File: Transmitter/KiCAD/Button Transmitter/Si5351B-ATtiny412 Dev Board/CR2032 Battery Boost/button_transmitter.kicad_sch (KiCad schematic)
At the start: 35 parts, among them J1 1.27mm Pogo Pads, J2 Conn_Coaxial, Q1 MMUN2238LT1G, U1 ATtiny412-SS, U2 Si5351B-B-GM1, U3 TLV61070ADBV, Y1 25MHz

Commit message: Finished CR2032 PCB layout
I like this. This is good
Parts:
- removed BZ1: Buzzer Pads, Jumper:SolderJumper-2_P1.3mm_Open_RoundedPad1.0x1.5mm, symbol Device:Buzzer
- removed D2: LS0504EVT233, Package_TO_SOT_SMD:SOT-23-3, symbol Power_Protection:CM1213A-01SO
- removed U1: ATtiny412-SS, Package_SO:SOIC-8_3.9x4.9mm_P1.27mm, symbol MCU_Microchip_ATtiny:ATtiny412-SS
- added BZ1: 7BB-20-3, Library:Buzzer_Pad_POS, symbol library:Buzzer_Pad_POS
- added BZ2-1: 7BB-20-3, Library:Buzzer_Pad_NEG, symbol library:Buzzer_Pad_NEG
- added C7: 100nF, Library:Worthington_C_0402_1005Metric, symbol Device:C_Small
- added D2: ESD156B1W, Diode_SMD:D_0201_0603Metric, symbol Device:D_TVS
- added U1: TPS22919DCK, Package_TO_SOT_SMD:SOT-363_SC-70-6, symbol library:TPS22919DCK
- added U3: ATtiny416-M, Package_DFN_QFN:VQFN-20-1EP_3x3mm_P0.4mm_EP1.7x1.7mm, symbol MCU_Microchip_ATtiny:ATtiny416-M
- BT1: footprint Battery:BatteryHolder_Keystone_3034_1x20mm -> Library:BatteryHolder_Keystone_3034_1x20mm_CUTOUT
- C1: renamed from C3; footprint Resistor_SMD:R_0402_1005Metric -> Library:Worthington_C_0402_1005Metric
- C10: renamed from C9; footprint Resistor_SMD:R_0603_1608Metric -> Capacitor_SMD:C_0603_1608Metric
- C2: renamed from C4; footprint Resistor_SMD:R_0402_1005Metric -> Library:Worthington_C_0402_1005Metric
- C3: renamed from C5; footprint Resistor_SMD:R_0402_1005Metric -> Library:Worthington_C_0402_1005Metric
- C4: renamed from C1; footprint Resistor_SMD:R_0402_1005Metric -> Library:Worthington_C_0402_1005Metric
- C5: renamed from C2; footprint Resistor_SMD:R_0402_1005Metric -> Library:Worthington_C_0402_1005Metric
- C6: renamed from C7; footprint Resistor_SMD:R_0402_1005Metric -> Library:Worthington_C_0402_1005Metric
- C8: renamed from C6; footprint Resistor_SMD:R_0402_1005Metric -> Library:Worthington_C_0402_1005Metric
- C9: renamed from C10; footprint Resistor_SMD:R_0402_1005Metric -> Library:Worthington_C_0402_1005Metric
- D1, D3: footprint LED_SMD:LED_0402_1005Metric -> Library:Worthington_LED_0402_1005Metric
- J1: renamed from J2; value Conn_Coaxial -> Antenna Screw Pad
- J2: renamed from J1; value 1.27mm Pogo Pads -> 1.27mm Pogo Pads For Programming & Debug
- L1: value 220uH -> 100mH; footprint Inductor_SMD:L_1008_2520Metric -> Inductor_THT:L_Axial_L12.0mm_D5.0mm_P15.24mm_Horizontal_Fastron_MISC; Field5 (none) -> B82144A2107J000
- R1: renamed from R4; footprint Resistor_SMD:R_0402_1005Metric -> Library:Worthington_R_0402_1005Metric
- R10, R11, R5, R6, R7, R9: footprint Resistor_SMD:R_0402_1005Metric -> Library:Worthington_R_0402_1005Metric
- R3: renamed from R2; footprint Resistor_SMD:R_0402_1005Metric -> Resistor_SMD:R_0603_1608Metric
- R4: renamed from R3; footprint Resistor_SMD:R_0402_1005Metric -> Library:Worthington_R_0402_1005Metric
- R8: value 100 -> 220; footprint Resistor_SMD:R_0402_1005Metric -> Library:Worthington_R_0402_1005Metric
- U4: value ~ -> Case
- renumbered R1 to R2, U3 to U5
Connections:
- net +3V3: now also U1.1 (VIN), U3.4 (VCC); no longer C1.1, C2.1, C3.1, L1.2, R2.1, R3.1, U2.11 (VDDOD), U2.14 (VDDOC), U2.16 (VDD), U2.8 (VDDOB), U2.9 (VDDOA)
- net GND: now also BZ2-1.2 (-), C7.1, D2.1 (A1), U1.2 (GND), U3.21 (GND), U3.3 (GND)
- net MCU_DAC0: now also C7.2, U3.7 (PA6)
- net MCU_SCL: now also R2.2, U3.14 (PB0); no longer R3.2
- net MCU_SDA: now also R3.2, U3.13 (PB1); no longer R2.2
- net MCU_UPDI: now also U3.19 (~{RESET}/PA0)
- net ~{TX_EN}: now also U3.12 (PB2)
- net at C6.2, R1.1: now also BZ1.1 (+)
- net at C9.1, L2.1, U5.3 (EN)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: now also BT1.1 (+), D2.2 (A2)
- net CLK1_T: now reaches U2.7 (CLK1)
- net CLK1_T: now also R4.1
- net BUZZER_PULSE: now reaches D1.2 (A), R6.1
- net BUZZER_PULSE: now also U3.17 (PC2)
- net CLK3 renamed CLK1
- net CLK3_T: no longer names the net of U2.12 (CLK3)
- net CLK3_T: no longer R4.1
- new net +3V3_SW: C1.1, C2.1, C3.1, L1.2, R2.1, R3.1, U1.5 (QOD), U1.6 (VOUT), U2.11 (VDDOD), U2.14 (VDDOC), U2.16 (VDD), U2.8 (VDDOB), U2.9 (VDDOA)
- new net OUTPUT_PWR_EN: U1.3 (ON), U3.6 (PA5)
- no-connect marks 3 -> 14
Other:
- note added: "1/[2*pi*sqrt(L*C)]"
- note added: "20nF Capacitance"
- note added: "3.6kHz"
- moved on the sheet: BT1, C1, C2, C3, C4, C5, C6, C8, D1, J1, J2, L1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

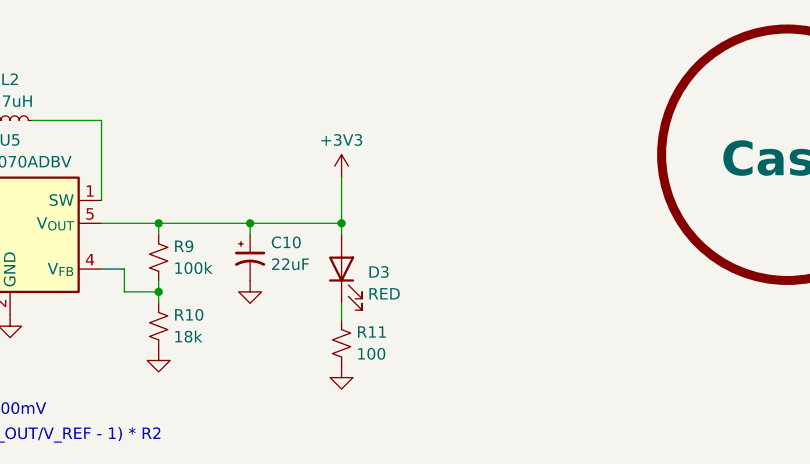
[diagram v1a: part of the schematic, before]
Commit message: Corrected BOM
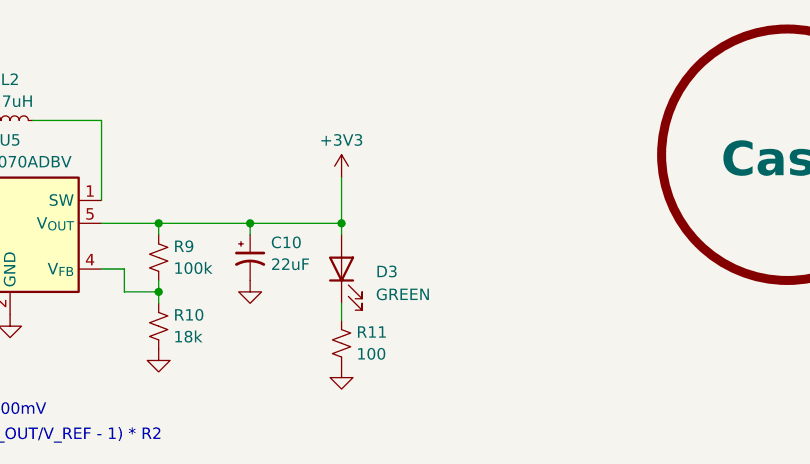
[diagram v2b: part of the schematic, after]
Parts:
- D3: value RED -> GREEN
- J1, J2, U4: now left out of the parts list
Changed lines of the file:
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@@
 	(label "CLK1_T"
 		(at 190.5 48.26 0)
-		(fields_autoplaced yes)
 		(effects
 			(font
@@
 	(label "MCU_UPDI"
 		(at 57.15 45.72 0)
-		(fields_autoplaced yes)
 		(effects
 			(font
@@
 	(label "MCU_DAC0"
 		(at 58.42 120.65 180)
-		(fields_autoplaced yes)
 		(effects
 			(font
@@
 	(label "OUTPUT_PWR_EN"
 		(at 82.55 34.29 180)
-		(fields_autoplaced yes)
 		(effects
 			(font
@@
 	(label "+3V3_SW"
 		(at 115.57 29.21 0)
-		(fields_autoplaced yes)
 		(effects
 			(font
@@
 	(label "MCU_SCL"
 		(at 71.12 118.11 0)
-		(fields_autoplaced yes)
 		(effects
 			(font
@@
 	(label "OUTPUT_PWR_EN"
 		(at 57.15 58.42 0)
-		(fields_autoplaced yes)
 		(effects
 			(font
@@
 	(label "MCU_SCL"
 		(at 160.02 50.8 180)
-		(fields_autoplaced yes)
 		(effects
 			(font
@@
 	(label "~{TX_EN}"
 		(at 57.15 73.66 0)
-		(fields_autoplaced yes)
 		(effects
 			(font
@@
 	(label "BUZZER_PULSE"
 		(at 220.98 99.06 180)
-		(fields_autoplaced yes)
 		(effects
 			(font
@@
 	(label "BUZZER_PULSE"
 		(at 57.15 91.44 0)
-		(fields_autoplaced yes)
 		(effects
 			(font
@@
 	(label "~{TX_EN}"
 		(at 159.385 76.2 180)
-		(fields_autoplaced yes)
 		(effects
 			(font
@@
 	(label "MCU_SCL"
 		(at 57.15 68.58 0)
-		(fields_autoplaced yes)
 		(effects
 			(font
@@
 	(label "MCU_SDA"
 		(at 58.42 118.11 180)
-		(fields_autoplaced yes)
 		(effects
 			(font
@@
 	(label "CLK1"
 		(at 208.915 48.26 0)
-		(fields_autoplaced yes)
 		(effects
 			(font
@@
 	(label "MCU_DAC0"
 		(at 160.02 55.88 180)
-		(fields_autoplaced yes)
 		(effects
 			(font
@@
 	(label "MCU_SDA"
 		(at 57.15 71.12 0)
-		(fields_autoplaced yes)
 		(effects
 			(font
@@
 	(label "MCU_SDA"
 		(at 160.02 48.26 180)
-		(fields_autoplaced yes)
 		(effects
 			(font
@@
 	(label "MCU_DAC0"
 		(at 57.15 60.96 0)
-		(fields_autoplaced yes)
 		(effects
 			(font
@@
 	(label "MCU_UPDI"
 		(at 58.42 115.57 180)
-		(fields_autoplaced yes)
 		(effects
 			(font
@@
 		(unit 1)
 		(exclude_from_sim no)
-		(in_bom yes)
+		(in_bom no)
 		(on_board yes)
 		(dnp no)
@@
 		(fields_autoplaced yes)
 		(property "Reference" "D3"
-			(at 147.701 156.5854 90)
+			(at 148.59 156.5274 90)
 			(effects
 				(font
@@
 			)
 		)
-		(property "Value" "RED"
-			(at 147.701 159.0096 90)
+		(property "Value" "GREEN"
+			(at 148.59 159.0674 90)
 			(effects
 				(font
@@
 		(unit 1)
 		(exclude_from_sim no)
-		(in_bom yes)
+		(in_bom no)
 		(on_board yes)
 		(dnp no)
@@
 		(unit 1)
 		(exclude_from_sim no)
-		(in_bom yes)
+		(in_bom no)
 		(on_board yes)
 		(dnp no)
